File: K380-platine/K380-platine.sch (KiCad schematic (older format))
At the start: 33 parts, among them J1 JST-PH 2, J2 Conn_01x23, J3 MicroMod-M.2E, J4 USB_C_Receptacle_USB2.0, J5 Conn_ARM_JTAG_SWD_10, Q1 PMost Enc FET -20V, Q2 Q_NMOS_DGS, SW1 EG1215AA, SW2 SW_Push, SW3 SW_Push, U1 XC6220B331MR, U2 MCP73831-2-OT

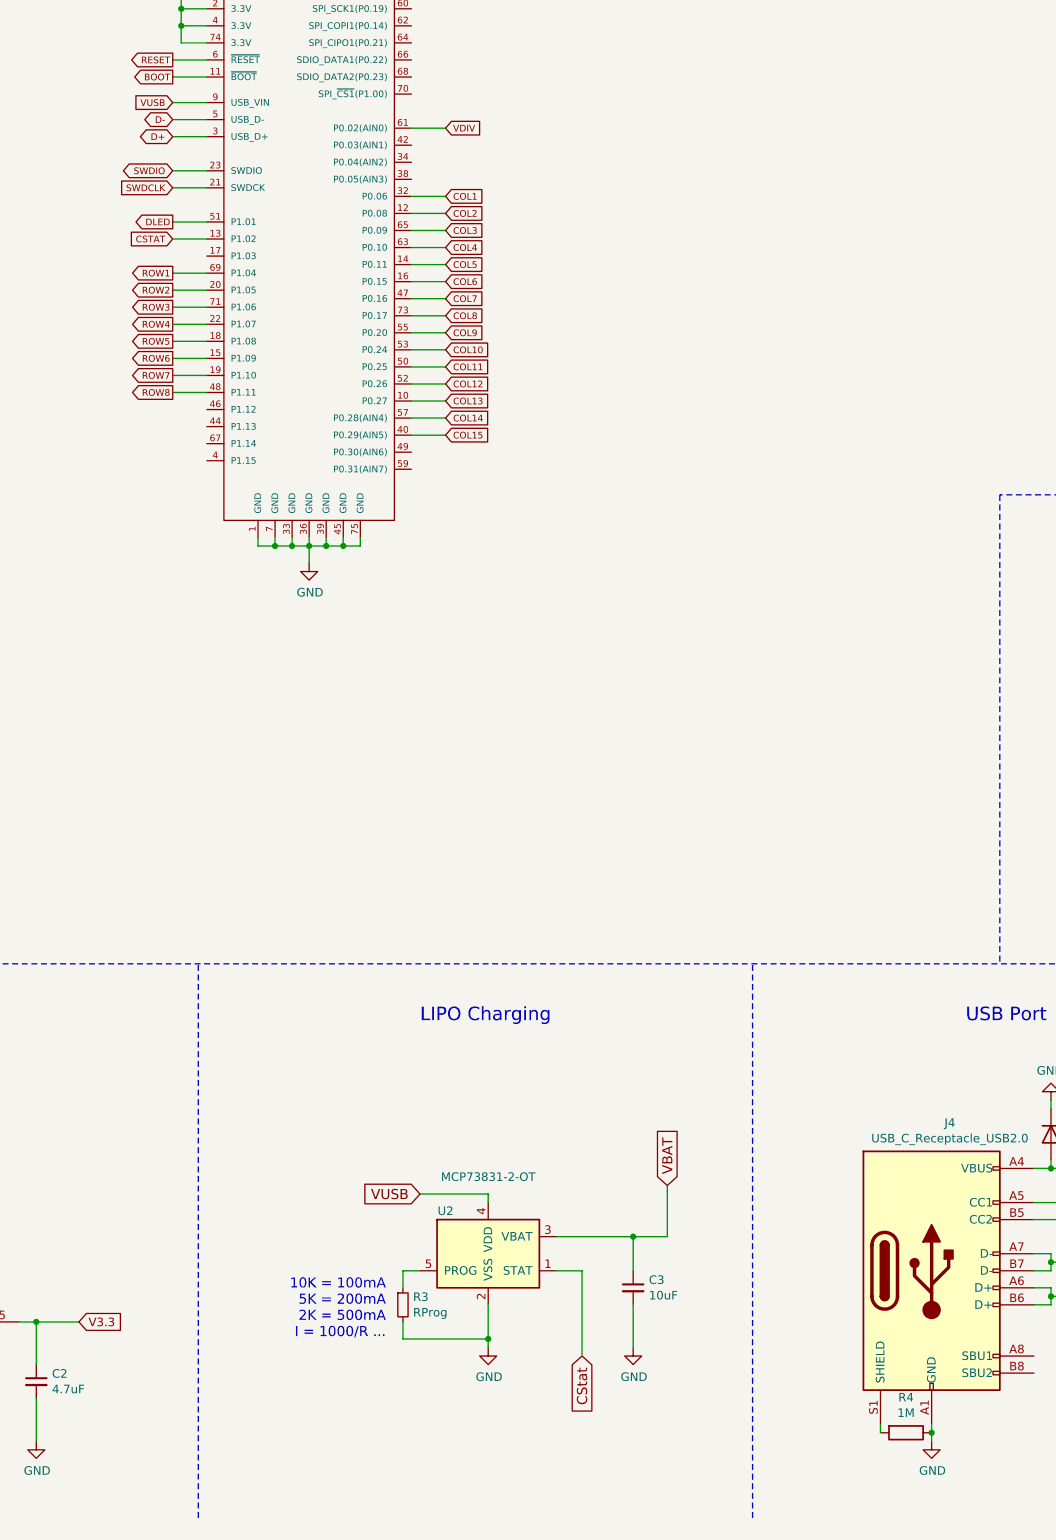
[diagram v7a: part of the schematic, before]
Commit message: Reordered keyboard matrix pins
- layout traces isn't as random as before
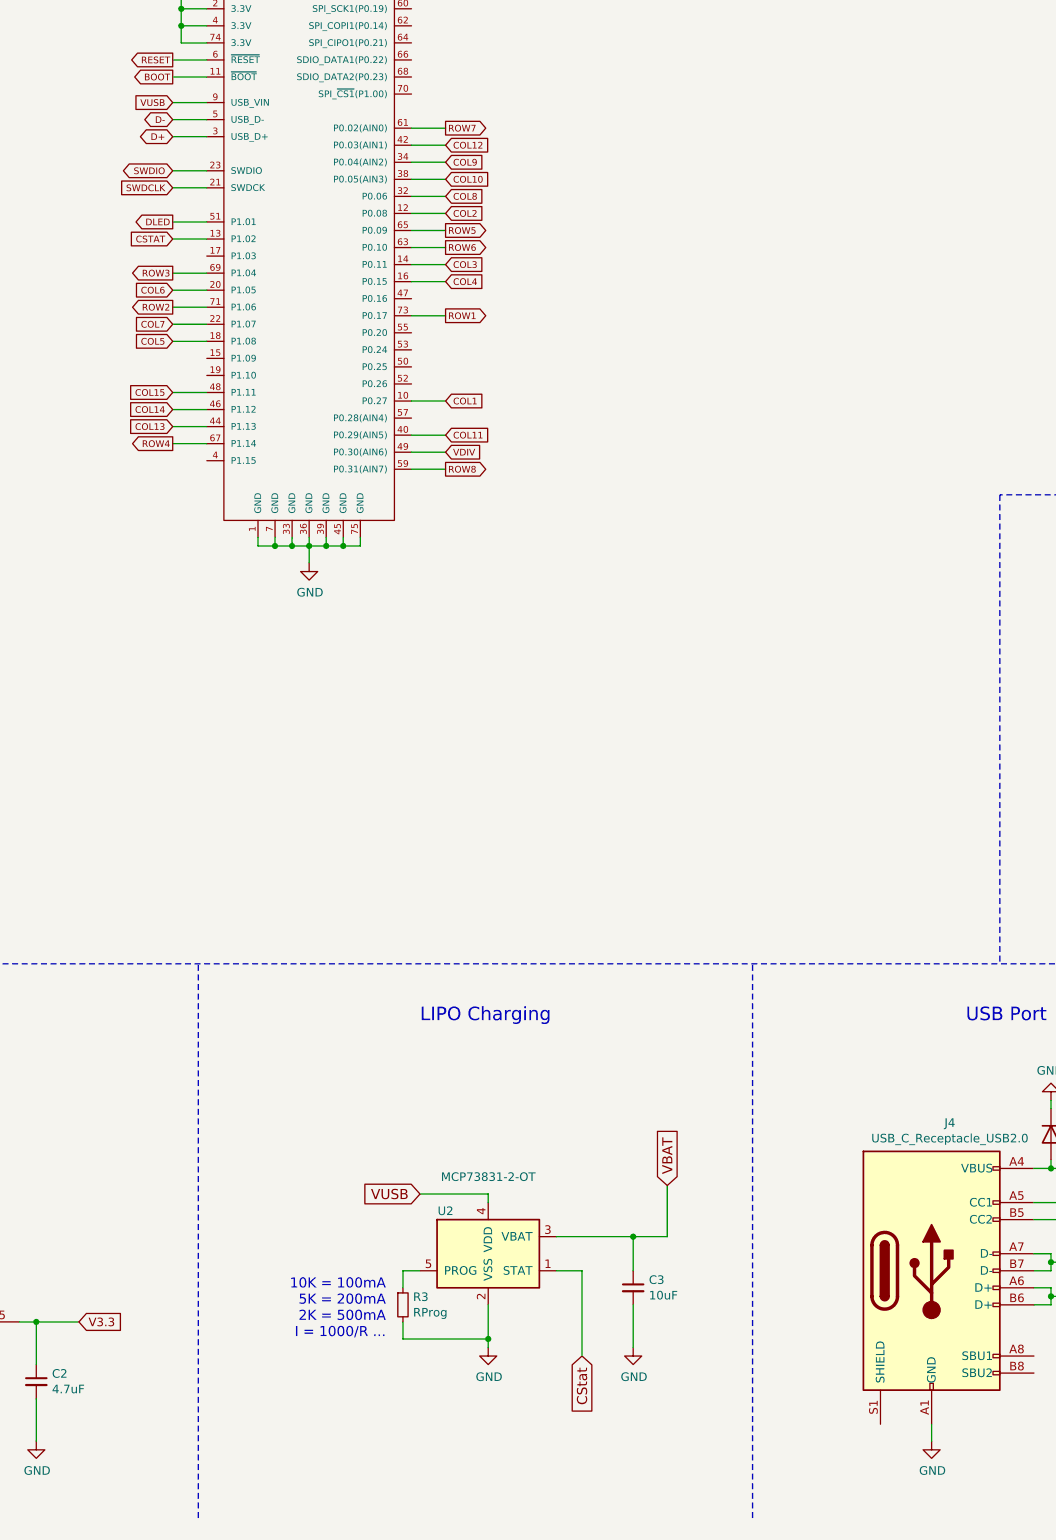
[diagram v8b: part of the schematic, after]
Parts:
- removed R4: 1M, Resistor_SMD:R_0805_2012Metric_Pad1.20x1.40mm_HandSolder, symbol Device:R
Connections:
- net COL1: now also J3.10 (P0.27); no longer J3.32 (P0.06)
- net COL10: now also J3.38 (P0.05(AIN3)); no longer J3.53 (P0.24)
- net COL11: now also J3.40 (P0.29(AIN5)); no longer J3.50 (P0.25)
- net COL12: now also J3.42 (P0.03(AIN1)); no longer J3.52 (P0.26)
- net COL13: now also J3.44 (P1.13); no longer J3.10 (P0.27)
- net COL14: now also J3.46 (P1.12); no longer J3.57 (P0.28(AIN4))
- net COL15: now also J3.48 (P1.11); no longer J3.40 (P0.29(AIN5))
- net COL3: now also J3.14 (P0.11); no longer J3.65 (P0.09)
- net COL4: now also J3.16 (P0.15); no longer J3.63 (P0.10)
- net COL5: now also J3.18 (P1.08); no longer J3.14 (P0.11)
- net COL6: now also J3.20 (P1.05); no longer J3.16 (P0.15)
- net COL7: now also J3.22 (P1.07); no longer J3.47 (P0.16)
- net COL8: now also J3.32 (P0.06); no longer J3.73 (P0.17)
- net COL9: now also J3.34 (P0.04(AIN2)); no longer J3.55 (P0.20)
- net ROW1: now also J3.73 (P0.17); no longer J3.69 (P1.04)
- net ROW2: now also J3.71 (P1.06); no longer J3.20 (P1.05)
- net ROW3: now also J3.69 (P1.04); no longer J3.71 (P1.06)
- net ROW4: now also J3.67 (P1.14); no longer J3.22 (P1.07)
- net ROW5: now also J3.65 (P0.09); no longer J3.18 (P1.08)
- net ROW6: now also J3.63 (P0.10); no longer J3.15 (P1.09)
- net ROW7: now also J3.61 (P0.02(AIN0)); no longer J3.19 (P1.10)
- net ROW8: now also J3.59 (P0.31(AIN7)); no longer J3.48 (P1.11)
- net VDIV: now also J3.49 (P0.30(AIN6)); no longer J3.61 (P0.02(AIN0))
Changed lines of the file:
@@
 	0    1    1    0
 $EndComp
-Wire Wire Line
-	8650 10650 8650 10700
-$Comp
-L Device:R R4
-U 1 1 62957FD7
-P 8500 10700
-F 0 "R4" V 8293 10700 50  0000 C CNN
-F 1 "1M" V 8384 10700 50  0000 C CNN
-F 2 "Resistor_SMD:R_0805_2012Metric_Pad1.20x1.40mm_HandSolder" V 8430 10700 50  0001 C CNN
-F 3 "~" H 8500 10700 50  0001 C CNN
-	1    8500 10700
-	0    1    1    0
-$EndComp
-Connection ~ 8650 10700
-Wire Wire Line
-	8650 10700 8650 10750
-Wire Wire Line
-	8350 10700 8350 10650
 $Comp
 L Device:R R5
@@
 Wire Wire Line
 	4400 3400 4200 3400
-Text GLabel 5800 3050 2    39   Input ~ 0
+Text GLabel 5800 4950 2    39   Input ~ 0
 VDIV
-Wire Wire Line
-	5800 3050 5600 3050
 Text GLabel 4200 3600 0    39   Output ~ 0
 DLED
-Wire Wire Line
-	4400 3600 4200 3600
 Text GLabel 4200 3700 0    39   Input ~ 0
 CSTAT
-Wire Wire Line
-	4200 3700 4400 3700
+Text GLabel 5800 4150 2    39   Output ~ 0
+ROW1
+Text GLabel 4200 4100 0    39   Output ~ 0
+ROW2
 Text GLabel 4200 3900 0    39   Output ~ 0
-ROW1
-Text GLabel 4200 4000 0    39   Output ~ 0
-ROW2
-Text GLabel 4200 4100 0    39   Output ~ 0
 ROW3
-Text GLabel 4200 4200 0    39   Output ~ 0
+Text GLabel 4200 4900 0    39   Output ~ 0
 ROW4
-Text GLabel 4200 4300 0    39   Output ~ 0
+Text GLabel 5800 3650 2    39   Output ~ 0
 ROW5
-Text GLabel 4200 4400 0    39   Output ~ 0
+Text GLabel 5800 3750 2    39   Output ~ 0
 ROW6
-Text GLabel 4200 4500 0    39   Output ~ 0
+Text GLabel 5800 3050 2    39   Output ~ 0
 ROW7
-Text GLabel 4200 4600 0    39   Output ~ 0
+Text GLabel 5800 5050 2    39   Output ~ 0
 ROW8
-Wire Wire Line
-	4200 3900 4400 3900
-Wire Wire Line
-	4400 4000 4200 4000
-Wire Wire Line
-	4200 4100 4400 4100
-Wire Wire Line
-	4400 4200 4200 4200
-Wire Wire Line
-	4200 4300 4400 4300
-Wire Wire Line
-	4400 4400 4200 4400
-Wire Wire Line
-	4200 4500 4400 4500
-Wire Wire Line
-	4400 4600 4200 4600
-Text GLabel 5800 3450 2    39   Input ~ 0
+Text GLabel 5800 4650 2    39   Input ~ 0
 COL1
 Text GLabel 5800 3550 2    39   Input ~ 0
 COL2
-Text GLabel 5800 3650 2    39   Input ~ 0
+Text GLabel 5800 3850 2    39   Input ~ 0
 COL3
-Text GLabel 5800 3750 2    39   Input ~ 0
+Text GLabel 5800 3950 2    39   Input ~ 0
 COL4
-Text GLabel 5800 3850 2    39   Input ~ 0
+Text GLabel 4200 4300 0    39   Input ~ 0
 COL5
-Text GLabel 5800 3950 2    39   Input ~ 0
+Text GLabel 4200 4000 0    39   Input ~ 0
 COL6
-Text GLabel 5800 4050 2    39   Input ~ 0
+Text GLabel 4200 4200 0    39   Input ~ 0
 COL7
-Text GLabel 5800 4150 2    39   Input ~ 0
+Text GLabel 5800 3450 2    39   Input ~ 0
 COL8
-Text GLabel 5800 4250 2    39   Input ~ 0
+Text GLabel 5800 3250 2    39   Input ~ 0
 COL9
-Text GLabel 5800 4350 2    39   Input ~ 0
+Text GLabel 5800 3350 2    39   Input ~ 0
 COL10
-Text GLabel 5800 4450 2    39   Input ~ 0
+Text GLabel 5800 4850 2    39   Input ~ 0
 COL11
-Text GLabel 5800 4550 2    39   Input ~ 0
+Text GLabel 5800 3150 2    39   Input ~ 0
 COL12
-Text GLabel 5800 4650 2    39   Input ~ 0
+Text GLabel 4200 4800 0    39   Input ~ 0
 COL13
-Text GLabel 5800 4750 2    39   Input ~ 0
+Text GLabel 4200 4700 0    39   Input ~ 0
 COL14
-Text GLabel 5800 4850 2    39   Input ~ 0
+Text GLabel 4200 4600 0    39   Input ~ 0
 COL15
-Wire Wire Line
-	5600 3450 5800 3450
-Wire Wire Line
-	5800 3550 5600 3550
-Wire Wire Line
-	5600 3650 5800 3650
-Wire Wire Line
-	5800 3750 5600 3750
-Wire Wire Line
-	5600 3850 5800 3850
-Wire Wire Line
-	5800 3950 5600 3950
-Wire Wire Line
-	5600 4050 5800 4050
-Wire Wire Line
-	5800 4150 5600 4150
-Wire Wire Line
-	5600 4250 5800 4250
-Wire Wire Line
-	5800 4350 5600 4350
-Wire Wire Line
-	5600 4450 5800 4450
-Wire Wire Line
-	5600 4550 5800 4550
-Wire Wire Line
-	5800 4650 5600 4650
-Wire Wire Line
-	5600 4750 5800 4750
-Wire Wire Line
-	5800 4850 5600 4850
 $Comp
 L power:GND #PWR011
@@
 Wire Wire Line
 	5100 5500 5200 5500
+Wire Wire Line
+	8650 10650 8650 10750
+Wire Wire Line
+	4200 3600 4400 3600
+Wire Wire Line
+	4400 3700 4200 3700
+Wire Wire Line
+	4200 3900 4400 3900
+Wire Wire Line
+	4400 4000 4200 4000
+Wire Wire Line
+	4200 4100 4400 4100
+Wire Wire Line
+	4400 4200 4200 4200
+Wire Wire Line
+	4200 4300 4400 4300
+Wire Wire Line
+	4400 4600 4200 4600
+Wire Wire Line
+	4200 4700 4400 4700
+Wire Wire Line
+	4400 4800 4200 4800
+Wire Wire Line
+	4200 4900 4400 4900
+Wire Wire Line
+	5600 5050 5800 5050
+Wire Wire Line
+	5800 4950 5600 4950
+Wire Wire Line
+	5600 4850 5800 4850
+Wire Wire Line
+	5800 4650 5600 4650
+Wire Wire Line
+	5600 4150 5800 4150
+Wire Wire Line
+	5800 3950 5600 3950
+Wire Wire Line
+	5600 3850 5800 3850
+Wire Wire Line
+	5800 3750 5600 3750
+Wire Wire Line
+	5600 3650 5800 3650
+Wire Wire Line
+	5800 3550 5600 3550
+Wire Wire Line
+	5600 3450 5800 3450
+Wire Wire Line
+	5800 3350 5600 3350
+Wire Wire Line
+	5600 3250 5800 3250
+Wire Wire Line
+	5800 3150 5600 3150
+Wire Wire Line
+	5600 3050 5800 3050
 $EndSCHEMATC
